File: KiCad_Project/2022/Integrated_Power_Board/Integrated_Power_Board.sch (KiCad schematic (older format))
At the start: 2 parts

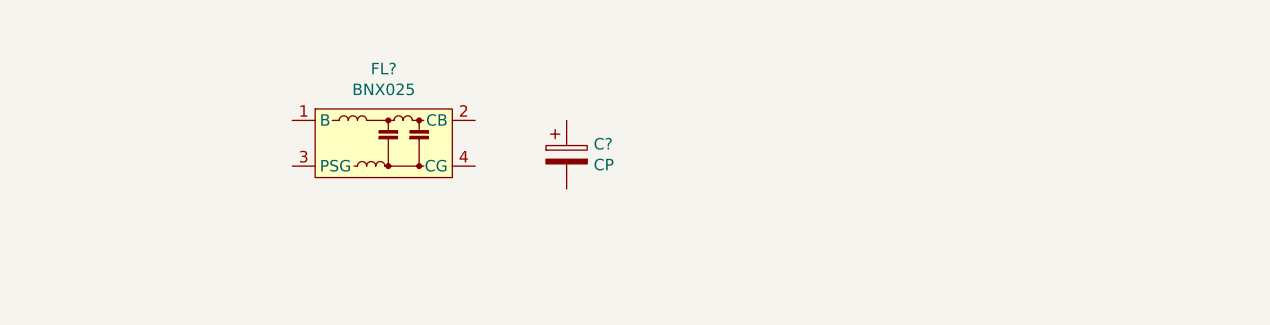
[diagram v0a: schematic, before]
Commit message: EMI対策とDCDCの周辺設計
過電流保護機能・加熱保護機能付き
可変抵抗で出力の変更可能
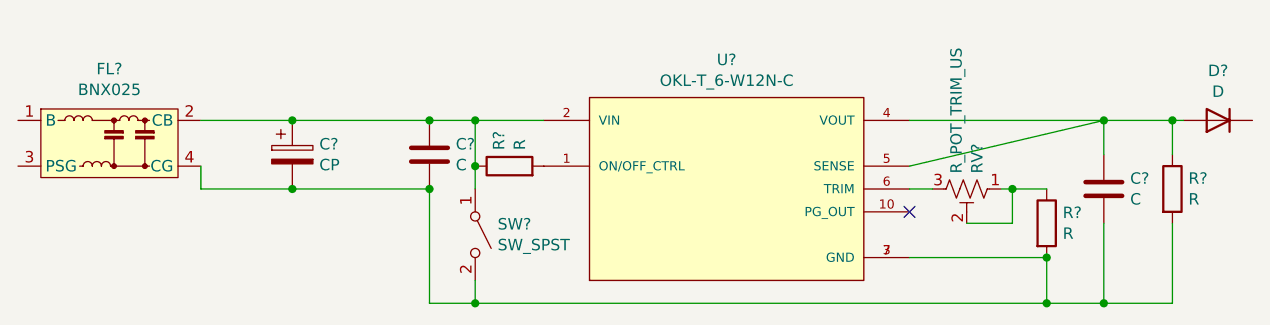
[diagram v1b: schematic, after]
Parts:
- added C? (x2): C, symbol Device:C
- added D?: D, symbol Device:D
- added R? (x3): R, symbol Device:R
- added RV?: R_POT_TRIM_US, symbol Device:R_POT_TRIM_US
- added SW?: SW_SPST, symbol Switch:SW_SPST
- added U?: OKL-T_6-W12N-C, CONV_OKL-T/6-W12N-C, symbol Converter_DCDC:OKL-T_6-W12N-C
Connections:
- net at FL?.2 (CB): now also C?.1, C?.1, R?.1, SW?.1 (A), U?.2 (VIN)
- net at FL?.4 (CG): now also C?.2, C?.2, C?.2, R?.2, R?.2, SW?.2 (B), U?.3 (GND), U?.7 (GND)
- new net: C?.1, D?.2 (A), R?.1, U?.4 (VOUT), U?.5 (SENSE)
- new net: R?.2, U?.1 (ON/OFF_CTRL)
- new net: RV?.3, U?.6 (TRIM)
- new net: R?.1, RV?.1, RV?.2
- no-connect marks 0 -> 1
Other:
- moved on the sheet: C?, FL?
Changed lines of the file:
@@
 L Filter:BNX025 FL?
 U 1 1 61E9826B
-P 6250 2450
-F 0 "FL?" H 6250 2775 50  0000 C CNN
-F 1 "BNX025" H 6250 2684 50  0000 C CNN
-F 2 "Filter:Filter_Murata_BNX025" H 6250 2250 50  0001 C CNN
-F 3 "https://www.murata.com/en-us/products/productdetail.aspx?cate=luNoiseSupprFilteBlockType&partno=BNX025H01%23" V 6225 2425 50  0001 C CNN
-	1    6250 2450
+P 5050 2450
+F 0 "FL?" H 5050 2775 50  0000 C CNN
+F 1 "BNX025" H 5050 2684 50  0000 C CNN
+F 2 "Filter:Filter_Murata_BNX025" H 5050 2250 50  0001 C CNN
+F 3 "https://www.murata.com/en-us/products/productdetail.aspx?cate=luNoiseSupprFilteBlockType&partno=BNX025H01%23" V 5025 2425 50  0001 C CNN
+	1    5050 2450
 	1    0    0    -1
 $EndComp
@@
 L Device:CP C?
 U 1 1 61E9D1C6
-P 7050 2500
-F 0 "C?" H 7168 2546 50  0000 L CNN
-F 1 "CP" H 7168 2455 50  0000 L CNN
-F 2 "" H 7088 2350 50  0001 C CNN
-F 3 "~" H 7050 2500 50  0001 C CNN
-	1    7050 2500
+P 5850 2500
+F 0 "C?" H 5968 2546 50  0000 L CNN
+F 1 "CP" H 5968 2455 50  0000 L CNN
+F 2 "" H 5888 2350 50  0001 C CNN
+F 3 "~" H 5850 2500 50  0001 C CNN
+	1    5850 2500
 	1    0    0    -1
 $EndComp
+Wire Wire Line
+	5450 2350 5850 2350
+Wire Wire Line
+	5450 2550 5450 2650
+Wire Wire Line
+	5450 2650 5850 2650
+$Comp
+L Converter_DCDC:OKL-T_6-W12N-C U?
+U 1 1 61EADD40
+P 7750 2650
+F 0 "U?" H 7750 3215 50  0000 C CNN
+F 1 "OKL-T_6-W12N-C" H 7750 3124 50  0000 C CNN
+F 2 "CONV_OKL-T/6-W12N-C" H 7300 3100 50  0001 L BNN
+F 3 "" H 7750 2650 50  0001 L BNN
+	1    7750 2650
+	1    0    0    -1
+$EndComp
+Connection ~ 5850 2350
+$Comp
+L Device:D D?
+U 1 1 61EAA1B2
+P 9900 2350
+F 0 "D?" H 9900 2133 50  0000 C CNN
+F 1 "D" H 9900 2224 50  0000 C CNN
+F 2 "" H 9900 2350 50  0001 C CNN
+F 3 "~" H 9900 2350 50  0001 C CNN
+	1    9900 2350
+	-1   0    0    1
+$EndComp
+$Comp
+L Device:C C?
+U 1 1 61ECBA50
+P 9400 2650
+F 0 "C?" H 9515 2696 50  0000 L CNN
+F 1 "C" H 9515 2605 50  0000 L CNN
+F 2 "" H 9438 2500 50  0001 C CNN
+F 3 "~" H 9400 2650 50  0001 C CNN
+	1    9400 2650
+	1    0    0    -1
+$EndComp
+$Comp
+L Device:C C?
+U 1 1 61ECFE45
+P 6450 2500
+F 0 "C?" H 6565 2546 50  0000 L CNN
+F 1 "C" H 6565 2455 50  0000 L CNN
+F 2 "" H 6488 2350 50  0001 C CNN
+F 3 "~" H 6450 2500 50  0001 C CNN
+	1    6450 2500
+	1    0    0    -1
+$EndComp
+Wire Wire Line
+	5850 2350 6450 2350
+Connection ~ 6450 2350
+Wire Wire Line
+	6450 2350 6650 2350
+Wire Wire Line
+	6450 2650 6450 3150
+Wire Wire Line
+	5850 2650 6450 2650
+Connection ~ 5850 2650
+Connection ~ 6450 2650
+$Comp
+L Device:R R?
+U 1 1 61ED432C
+P 6800 2550
+F 0 "R?" H 6870 2596 50  0000 L CNN
+F 1 "R" H 6870 2505 50  0000 L CNN
+F 2 "" V 6730 2550 50  0001 C CNN
+F 3 "~" H 6800 2550 50  0001 C CNN
+	1    6800 2550
+	0    -1   -1   0
+$EndComp
+Wire Wire Line
+	6650 2550 6650 2350
+Connection ~ 6650 2350
+Wire Wire Line
+	6650 2350 6950 2350
+NoConn ~ 8550 2750
+Wire Wire Line
+	6450 3150 6650 3150
+$Comp
+L Switch:SW_SPST SW?
+U 1 1 61EDE86A
+P 6650 2850
+F 0 "SW?" V 6604 2948 50  0000 L CNN
+F 1 "SW_SPST" V 6695 2948 50  0000 L CNN
+F 2 "" H 6650 2850 50  0001 C CNN
+F 3 "~" H 6650 2850 50  0001 C CNN
+	1    6650 2850
+	0    1    1    0
+$EndComp
+Wire Wire Line
+	6650 3150 6650 3050
+Connection ~ 6650 3150
+Wire Wire Line
+	6650 3150 9150 3150
+Wire Wire Line
+	6650 2650 6650 2550
+Connection ~ 6650 2550
+Wire Wire Line
+	9400 2350 9400 2500
+$Comp
+L Device:R R?
+U 1 1 61EE2976
+P 9700 2650
+F 0 "R?" H 9770 2696 50  0000 L CNN
+F 1 "R" H 9770 2605 50  0000 L CNN
+F 2 "" V 9630 2650 50  0001 C CNN
+F 3 "~" H 9700 2650 50  0001 C CNN
+	1    9700 2650
+	1    0    0    -1
+$EndComp
+Wire Wire Line
+	9400 3150 9700 3150
+Wire Wire Line
+	9700 3150 9700 2800
+Wire Wire Line
+	9400 2350 9700 2350
+Wire Wire Line
+	9700 2500 9700 2350
+Connection ~ 9700 2350
+Wire Wire Line
+	9700 2350 9750 2350
+$Comp
+L Device:R_POT_TRIM_US RV?
+U 1 1 61EE7113
+P 8800 2650
+F 0 "RV?" H 8732 2696 50  0000 R CNN
+F 1 "R_POT_TRIM_US" H 8732 2605 50  0000 R CNN
+F 2 "" H 8800 2650 50  0001 C CNN
+F 3 "~" H 8800 2650 50  0001 C CNN
+	1    8800 2650
+	0    1    1    0
+$EndComp
+Wire Wire Line
+	9400 2800 9400 3150
+$Comp
+L Device:R R?
+U 1 1 61EF0CD5
+P 9150 2800
+F 0 "R?" H 9220 2846 50  0000 L CNN
+F 1 "R" H 9220 2755 50  0000 L CNN
+F 2 "" V 9080 2800 50  0001 C CNN
+F 3 "~" H 9150 2800 50  0001 C CNN
+	1    9150 2800
+	1    0    0    -1
+$EndComp
+Wire Wire Line
+	8950 2650 9000 2650
+Wire Wire Line
+	9000 2650 9000 2800
+Wire Wire Line
+	9000 2800 8800 2800
+Connection ~ 9000 2650
+Wire Wire Line
+	8550 2950 9150 2950
+Wire Wire Line
+	9000 2650 9150 2650
+Connection ~ 9150 2950
+Wire Wire Line
+	8550 2650 8650 2650
+Wire Wire Line
+	9150 3150 9150 2950
+Connection ~ 9400 2350
+Wire Wire Line
+	8550 2350 9400 2350
+Wire Wire Line
+	8550 2550 9400 2350
+Wire Wire Line
+	9150 3150 9400 3150
+Connection ~ 9150 3150
+Connection ~ 9400 3150
 $EndSCHEMATC

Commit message: 回路図の完成
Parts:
- added BT?: Battery, symbol Device:Battery
- added F?: Fuse, symbol Device:Fuse
- added J? (x5): Conn_01x02, symbol Connector_Generic:Conn_01x02
- added MES? (x2): Voltmeter_DC, symbol Device:Voltmeter_DC
- added RV?: Varistor, symbol Device:Varistor
- added SW?: Switch_SW_SPST, symbol Integrated_Power_Board-cache:Switch_SW_SPST
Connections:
- net +12V: now reaches FL?.1 (B)
- net +12V: now also RV?.1, SW?.2 (B)
- net GND: now reaches FL?.3 (PSG)
- net GND: now also BT?.1 (-), MES?.1 (-), RV?.2
- net GND1: now reaches C?.2, C?.2, C?.2, FL?.4 (CG), R?.2, R?.2, SW?.2 (B), U?.3 (GND), U?.7 (GND)
- net GND1: now also MES?.1 (-)
- net +5V: now reaches D?.1 (K)
- net +5V: now also MES?.2 (+)
- new net: BT?.2 (+), F?.2
- new net Voltage: F?.1, MES?.2 (+), SW?.1 (A)
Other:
- moved on the sheet: C?, D?, FL?, R?, RV?, SW?, U?

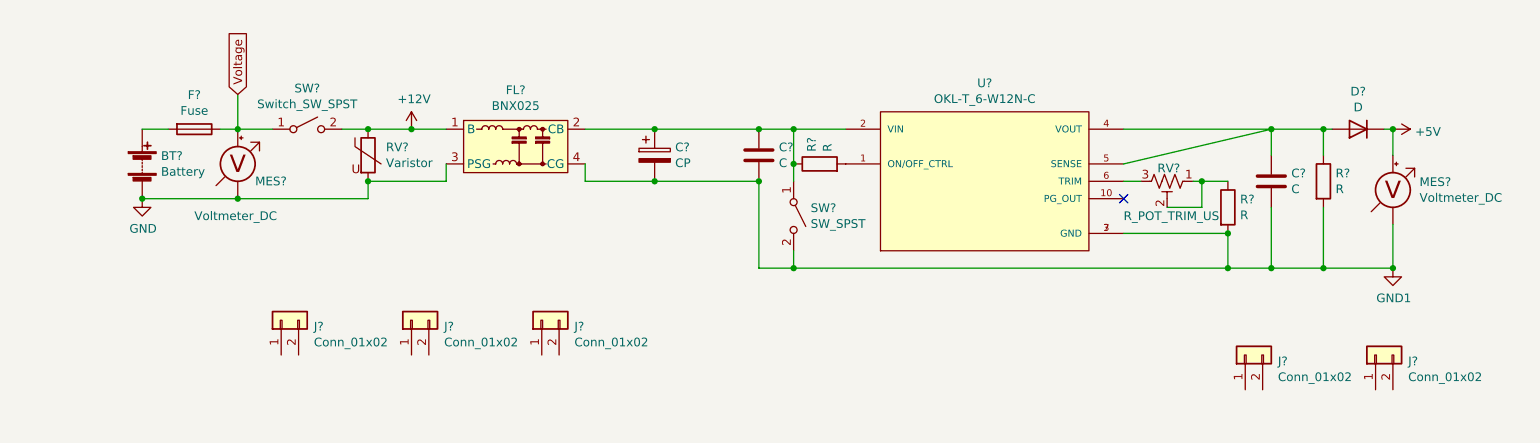
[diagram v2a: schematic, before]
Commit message: コネクタの逆差し対策
ショットキーバリスタダイオードでDCDCよりも前に素早く短絡させます
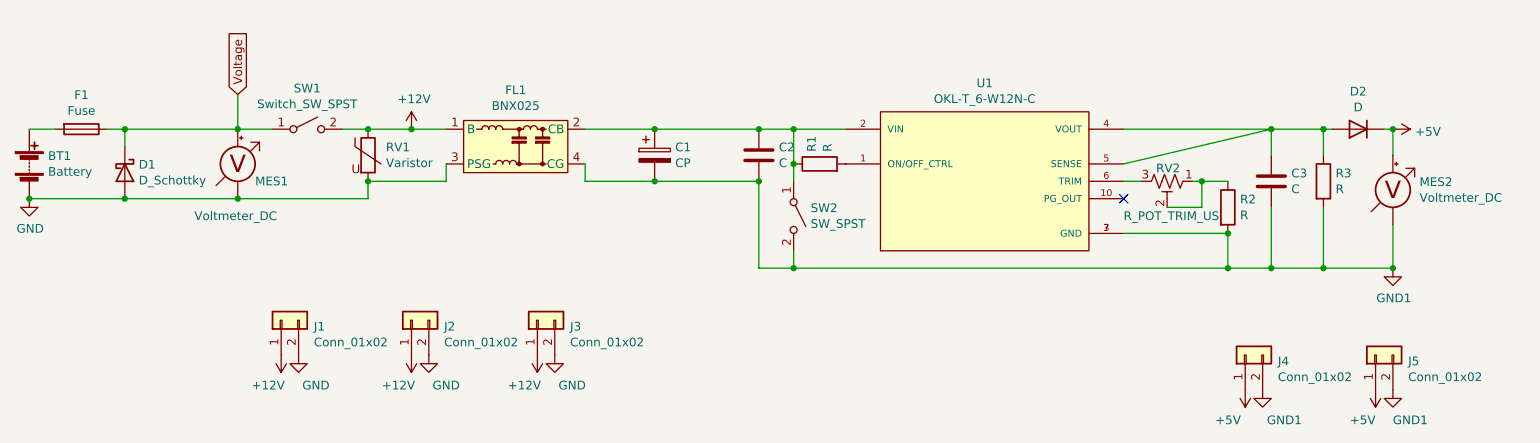
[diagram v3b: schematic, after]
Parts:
- removed J? (x2): Conn_01x02, symbol Connector_Generic:Conn_01x02
- added D1: D_Schottky, symbol Device:D_Schottky
- added J2, J3: Conn_01x02, symbol Connector_Generic:Conn_01x02
- gave numbers to parts that had none: 20
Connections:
- net +12V: now also J1.1 (Pin_1), J2.1 (Pin_1), J3.1 (Pin_1)
- net +5V: now also J4.1 (Pin_1), J5.1 (Pin_1)
- net GND: now also J1.2 (Pin_2), D1.2 (A), J2.2 (Pin_2), J3.2 (Pin_2)
- net GND1: now also J4.2 (Pin_2), J5.2 (Pin_2)
- net Voltage: now also D1.1 (K)
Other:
- moved on the sheet: BT1, F1

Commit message: 電源統合基板の進捗
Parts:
- removed D1: D_Schottky, symbol Device:D_Schottky
- removed MES2: Voltmeter_DC, symbol Device:Voltmeter_DC
- FL1: footprint Filter:Filter_Murata_BNX025 -> BNX016-01:FIL_BNX016-01
- J1, J2, J3, J4, J5: footprint (none) -> Connector_JST:JST_XH_B2B-XH-A_1x02_P2.50mm_Vertical
- U1: footprint CONV_OKL-T/6-W12N-C -> OKL-T_6-W12N-C:DCDC-murata-6A
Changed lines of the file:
@@
 F 0 "FL1" H 4500 2775 50  0000 C CNN
 F 1 "BNX025" H 4500 2684 50  0000 C CNN
-F 2 "Filter:Filter_Murata_BNX025" H 4500 2250 50  0001 C CNN
+F 2 "BNX016-01:FIL_BNX016-01" H 4500 2250 50  0001 C CNN
 F 3 "https://www.murata.com/en-us/products/productdetail.aspx?cate=luNoiseSupprFilteBlockType&partno=BNX025H01%23" V 4475 2425 50  0001 C CNN
 	1    4500 2450
@@
 F 0 "U1" H 7200 3215 50  0000 C CNN
 F 1 "OKL-T_6-W12N-C" H 7200 3124 50  0000 C CNN
-F 2 "CONV_OKL-T/6-W12N-C" H 6750 3100 50  0001 L BNN
+F 2 "OKL-T_6-W12N-C:DCDC-murata-6A" H 6750 3100 50  0001 L BNN
 F 3 "" H 7200 2650 50  0001 L BNN
 	1    7200 2650
@@
 Connection ~ 8600 3150
 Connection ~ 8850 3150
-$Comp
-L Device:Voltmeter_DC MES2
-U 1 1 61EAE85E
-P 9550 2700
-F 0 "MES2" H 9703 2746 50  0000 L CNN
-F 1 "Voltmeter_DC" H 9703 2655 50  0000 L CNN
-F 2 "" V 9550 2800 50  0001 C CNN
-F 3 "~" V 9550 2800 50  0001 C CNN
-	1    9550 2700
-	1    0    0    -1
-$EndComp
 Wire Wire Line
 	9150 3150 9550 3150
-Wire Wire Line
-	9550 3150 9550 2900
 Connection ~ 9150 3150
 Wire Wire Line
 	9500 2350 9550 2350
-Wire Wire Line
-	9550 2350 9550 2500
 $Comp
 L power:GND1 #PWR013
@@
 	1    0    0    -1
 $EndComp
-Connection ~ 9550 3150
 $Comp
 L power:+5V #PWR012
@@
 	0    1    1    0
 $EndComp
-Connection ~ 9550 2350
 $Comp
 L Device:Battery BT1
@@
 	3500 2350 3650 2350
 Connection ~ 3650 2350
-Wire Wire Line
-	2250 2750 1700 2750
 Connection ~ 1700 2750
 Text GLabel 2900 2150 1    50   Input ~ 0
@@
 F 0 "J1" V 3114 3262 50  0000 R CNN
 F 1 "Conn_01x02" V 3023 3262 50  0000 R CNN
-F 2 "" H 3150 3450 50  0001 C CNN
+F 2 "Connector_JST:JST_XH_B2B-XH-A_1x02_P2.50mm_Vertical" H 3150 3450 50  0001 C CNN
 F 3 "~" H 3150 3450 50  0001 C CNN
 	1    3150 3450
@@
 F 0 "J4" V 8664 3462 50  0000 R CNN
 F 1 "Conn_01x02" V 8573 3462 50  0000 R CNN
-F 2 "" H 8700 3650 50  0001 C CNN
+F 2 "Connector_JST:JST_XH_B2B-XH-A_1x02_P2.50mm_Vertical" H 8700 3650 50  0001 C CNN
 F 3 "~" H 8700 3650 50  0001 C CNN
 	1    8700 3650
@@
 F 0 "J5" V 9414 3462 50  0000 R CNN
 F 1 "Conn_01x02" V 9323 3462 50  0000 R CNN
-F 2 "" H 9450 3650 50  0001 C CNN
+F 2 "Connector_JST:JST_XH_B2B-XH-A_1x02_P2.50mm_Vertical" H 9450 3650 50  0001 C CNN
 F 3 "~" H 9450 3650 50  0001 C CNN
 	1    9450 3650
 	0    -1   -1   0
 $EndComp
-$Comp
-L Device:D_Schottky D1
-U 1 1 61EDC595
-P 2250 2600
-F 0 "D1" V 2204 2680 50  0000 L CNN
-F 1 "D_Schottky" V 2295 2680 50  0000 L CNN
-F 2 "" H 2250 2600 50  0001 C CNN
-F 3 "~" H 2250 2600 50  0001 C CNN
-	1    2250 2600
-	0    1    1    0
-$EndComp
-Wire Wire Line
-	2250 2750 2900 2750
-Connection ~ 2250 2750
 Connection ~ 2900 2750
-Wire Wire Line
-	2150 2350 2250 2350
-Wire Wire Line
-	2250 2450 2250 2350
-Connection ~ 2250 2350
-Wire Wire Line
-	2250 2350 2900 2350
 $Comp
 L power:+12V #PWR02
@@
 F 0 "J2" V 3864 3262 50  0000 R CNN
 F 1 "Conn_01x02" V 3773 3262 50  0000 R CNN
-F 2 "" H 3900 3450 50  0001 C CNN
+F 2 "Connector_JST:JST_XH_B2B-XH-A_1x02_P2.50mm_Vertical" H 3900 3450 50  0001 C CNN
 F 3 "~" H 3900 3450 50  0001 C CNN
 	1    3900 3450
@@
 F 0 "J3" V 4589 3262 50  0000 R CNN
 F 1 "Conn_01x02" V 4498 3262 50  0000 R CNN
-F 2 "" H 4625 3450 50  0001 C CNN
+F 2 "Connector_JST:JST_XH_B2B-XH-A_1x02_P2.50mm_Vertical" H 4625 3450 50  0001 C CNN
 F 3 "~" H 4625 3450 50  0001 C CNN
 	1    4625 3450
@@
 	-1   0    0    1
 $EndComp
+Wire Wire Line
+	1700 2750 2900 2750
+Wire Wire Line
+	2150 2350 2900 2350
 $EndSCHEMATC

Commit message: 電源統合基板の進捗
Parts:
- BT1: footprint (none) -> Connector_JST:JST_VH_B2P-VH-B_1x02_P3.96mm_Vertical
- F1: footprint (none) -> herakuresu2022:fuse_socket
- MES1: footprint (none) -> herakuresu2022:voltage_counter
- SW2: footprint (none) -> herakuresu2022:2MS1T2B4M2QES
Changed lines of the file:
@@
 F 0 "SW2" V 6054 2948 50  0000 L CNN
 F 1 "SW_SPST" V 6145 2948 50  0000 L CNN
-F 2 "" H 6100 2850 50  0001 C CNN
+F 2 "herakuresu2022:2MS1T2B4M2QES" H 6100 2850 50  0001 C CNN
 F 3 "~" H 6100 2850 50  0001 C CNN
 	1    6100 2850
@@
 F 0 "BT1" H 1808 2596 50  0000 L CNN
 F 1 "Battery" H 1808 2505 50  0000 L CNN
-F 2 "" V 1700 2610 50  0001 C CNN
+F 2 "Connector_JST:JST_VH_B2P-VH-B_1x02_P3.96mm_Vertical" V 1700 2610 50  0001 C CNN
 F 3 "~" V 1700 2610 50  0001 C CNN
 	1    1700 2550
@@
 F 0 "F1" V 1803 2350 50  0000 C CNN
 F 1 "Fuse" V 1894 2350 50  0000 C CNN
-F 2 "" V 1930 2350 50  0001 C CNN
+F 2 "herakuresu2022:fuse_socket" V 1930 2350 50  0001 C CNN
 F 3 "~" H 2000 2350 50  0001 C CNN
 	1    2000 2350
@@
 F 0 "MES1" H 3000 2450 50  0000 L CNN
 F 1 "Voltmeter_DC" H 2650 2250 50  0000 L CNN
-F 2 "" V 2900 2650 50  0001 C CNN
+F 2 "herakuresu2022:voltage_counter" V 2900 2650 50  0001 C CNN
 F 3 "~" V 2900 2650 50  0001 C CNN
 	1    2900 2550
